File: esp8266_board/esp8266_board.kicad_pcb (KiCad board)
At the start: 2 copper layers, 50 x 30 mm, 11 parts, among them J1 Screw_Terminal_01x04, J2 Conn_01x08_Pin, J3 Screw_Terminal_01x02, M2 MountingHole_2.2mm_M2, SW1 SW_Push, SW2 SW_Push

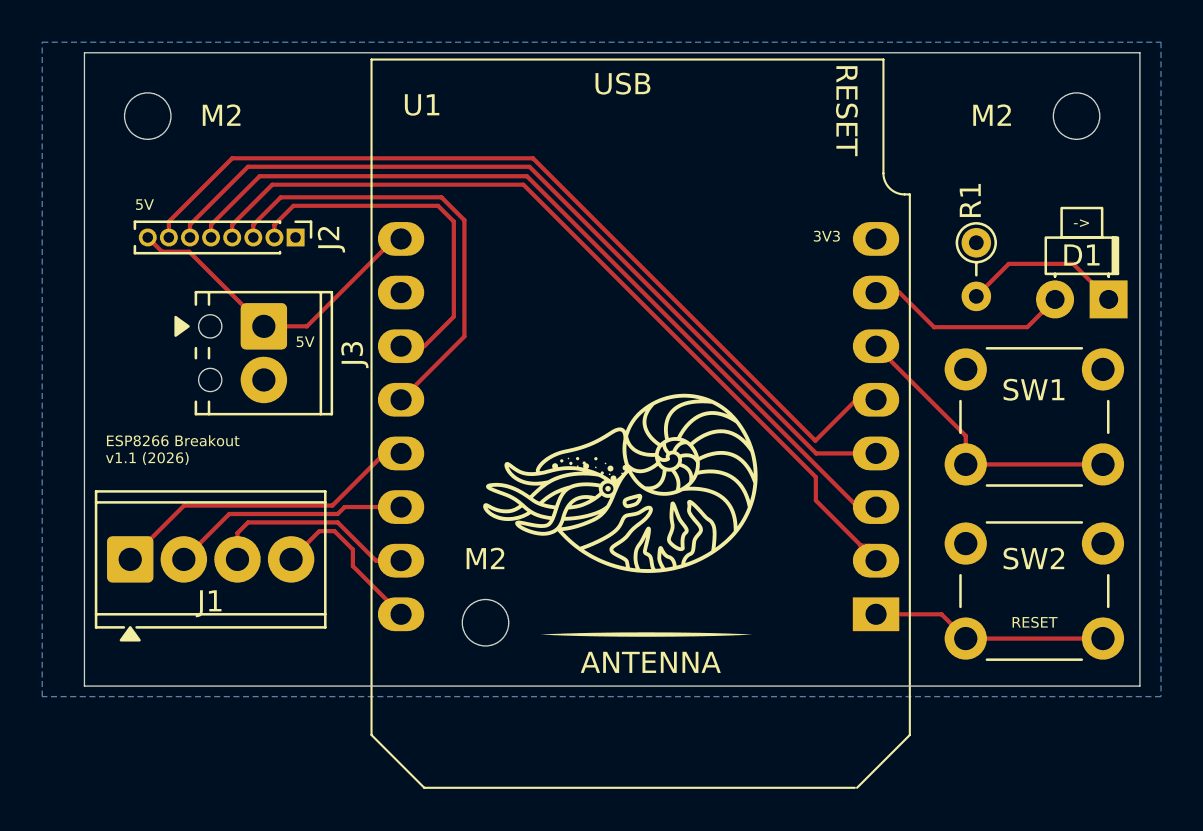
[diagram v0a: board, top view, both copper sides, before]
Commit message: Fixing component footprints, copper clearances, and refab
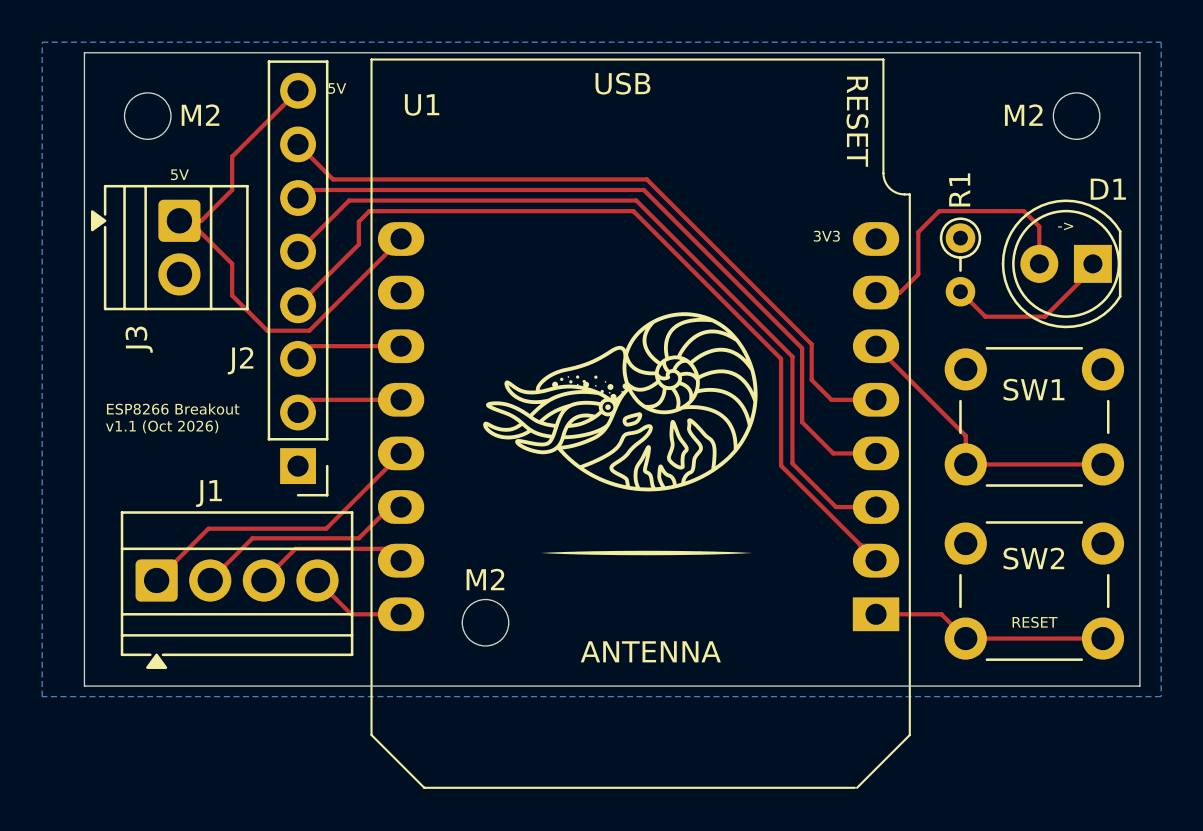
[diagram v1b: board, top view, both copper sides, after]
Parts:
- D1: footprint LED_THT:LED_D1.8mm_W1.8mm_H2.4mm_Horizontal_O1.27mm_Z1.6mm -> LED_THT:LED_D5.0mm
- J1: footprint TerminalBlock_Phoenix:TerminalBlock_Phoenix_MPT-0,5-4-2.54_1x04_P2.54mm_Horizontal -> TerminalBlock:TerminalBlock_Xinya_XY308-2.54-4P_1x04_P2.54mm_Horizontal
- J2: footprint Connector_PinHeader_1.00mm:PinHeader_1x08_P1.00mm_Vertical -> Connector_PinHeader_2.54mm:PinHeader_1x08_P2.54mm_Vertical
- J3: footprint TerminalBlock_Phoenix:TerminalBlock_Phoenix_MPT-0,5-2-2.54_1x02_P2.54mm_Horizontal -> TerminalBlock:TerminalBlock_Xinya_XY308-2.54-2P_1x02_P2.54mm_Horizontal
- moved J2 10.8 mm to (152.1, 63.6), turned to 180 degrees
- moved J3 6.40 mm to (146.5, 52.0)
- moved D1 1.84 mm to (189.8, 54.0)
- moved J1 1.60 mm to (145.4, 69.0)
- moved R1 0.78 mm to (183.5, 52.8)
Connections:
- U1 pad 11: Net-(J2-Pin_2) -> Net-(J2-Pin_3)
- U1 pad 12: Net-(J2-Pin_3) -> Net-(J2-Pin_2)
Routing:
- net Net-(J2-Pin_3): track 21.3 -> 5.13 mm
- net Net-(J2-Pin_2): track 17.4 -> 5.13 mm
- net Net-(J2-Pin_8): track 16.3 -> 25.3 mm
- net Net-(J2-Pin_7): track 41.8 -> 33.4 mm
- net Net-(J2-Pin_6): track 39.9 -> 34.8 mm
- net Net-(J1-Pin_4): track 7.86 -> 4.62 mm
- net Net-(D1-A): track 9.70 -> 12.6 mm
- net Net-(J1-Pin_3): track 9.96 -> 7.35 mm
- net Net-(J2-Pin_5): track 39.5 -> 37.4 mm
- net Net-(J1-Pin_2): track 11.3 -> 10.5 mm
- net Net-(J1-Pin_1): track 14.9 -> 14.1 mm
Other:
- board text added: "ESP8266 Breakout v1.1 (Oct 2026)"
- board text removed: "ESP8266 Breakout v1.1 (2026)"
